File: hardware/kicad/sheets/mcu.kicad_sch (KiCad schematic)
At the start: 44 parts, among them J1 USB-C, J14 QWIIC, J5 DISPLAY, J6 NAV_SW, J7 AUX, SW1 RESET, SW2 BOOT, U1 ESP32-S3-WROOM-1U-N16R2, U4 SRV05-4

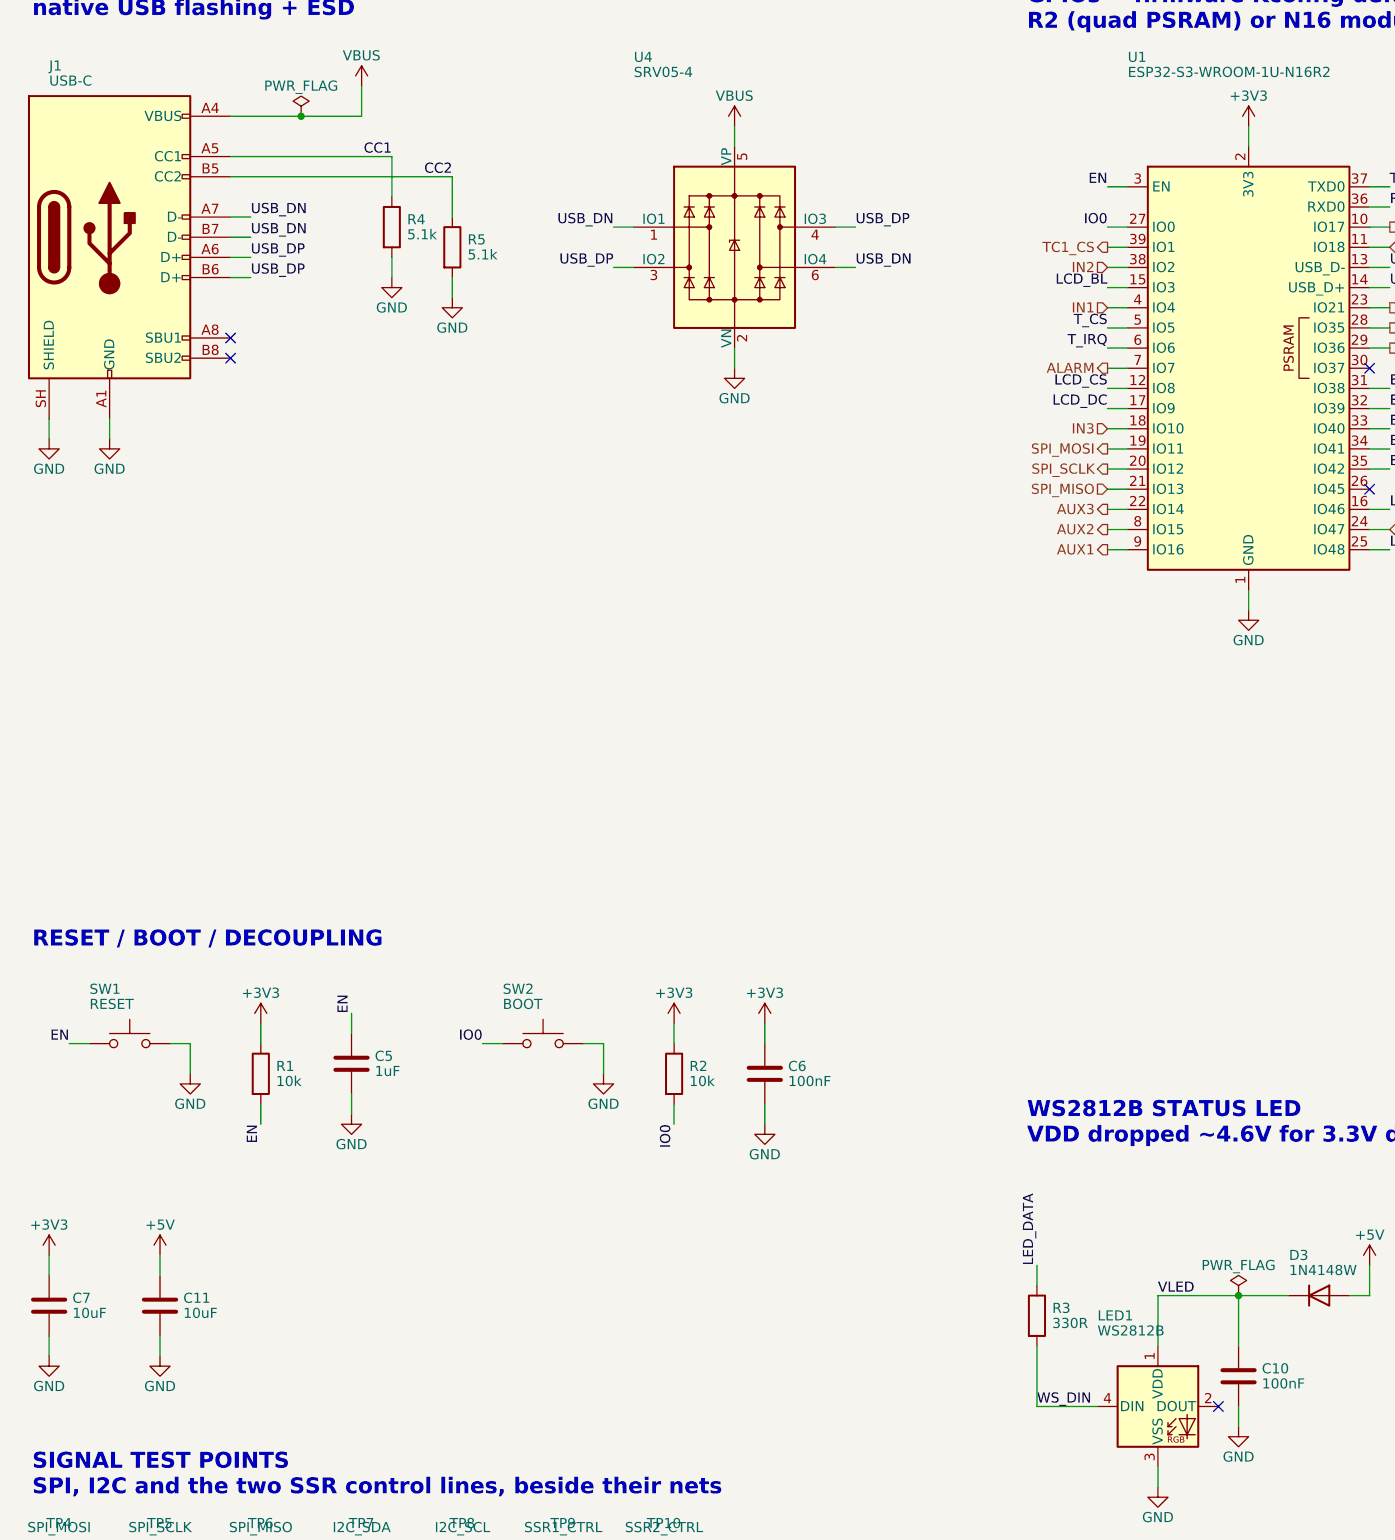
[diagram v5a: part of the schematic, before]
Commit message: hardware: inline front-ends and decoupling at the pins (review 12, 13)
Fourth batch from SCHEMATIC-REVIEW-2026-10-22.md.

Thermocouples: each MAX31856 front-end is an inline chain - the terminal
mirrored so its pins face the IC, K+ and K- on two lines through their
100R, the 100 nF differential cap bridging the lines, the 10 nF caps to
GND off each line, BIAS returned to the raw K- node along the bottom -
and AVDD/DVDD rise to a short +3V3 rail with both 100 nF hanging from
it. The ICs slid 7.62 mm right to make room; nothing else moved.

CT: J12 feeds four lines at 17.78 mm pitch with the 5R1 burden between
each pair, the 1k series parts in the path, the 33 nF to GND off each
filtered node and the 1k references off the N lines; the filtered nodes
end in the CTA_F / CTA_FN / CTB_F labels the ADE7953 pins already
carried. D6 keeps a label-fed clamp block beside the chain. VDD, VINTD
and VINTA each get a rail at the IC's top pin with their two caps on it;
R37/R38 moved 7.62 mm right to clear them.

io: IN1-IN3 are three identical rows - J11 mirrored, 1k in the path, the
10k pull-up above and 100 nF below the node, the hierarchical label at
the end - with D5's clamp block below them.

mcu: C6/C7 hang from U1's 3V3 pin. power: U2 is drawn as an inline
5 V -> 3.3 V chain with C1/C2 on its input and C3/C4 on its output in
the row the caps already occupied; LED2/R9 slid right.

Every pin landed on wiring by construction (the geometry helper checks
each symbol's pins against the wires), ERC is clean, the layout checker
reports no overlaps, the netlist still has 108 nets and the board sync
re-netted nothing. Fab outputs regenerated (schematic PDF, timestamps).

Co-Authored-By: Claude Fable 5.1 <noreply@anthropic.com>
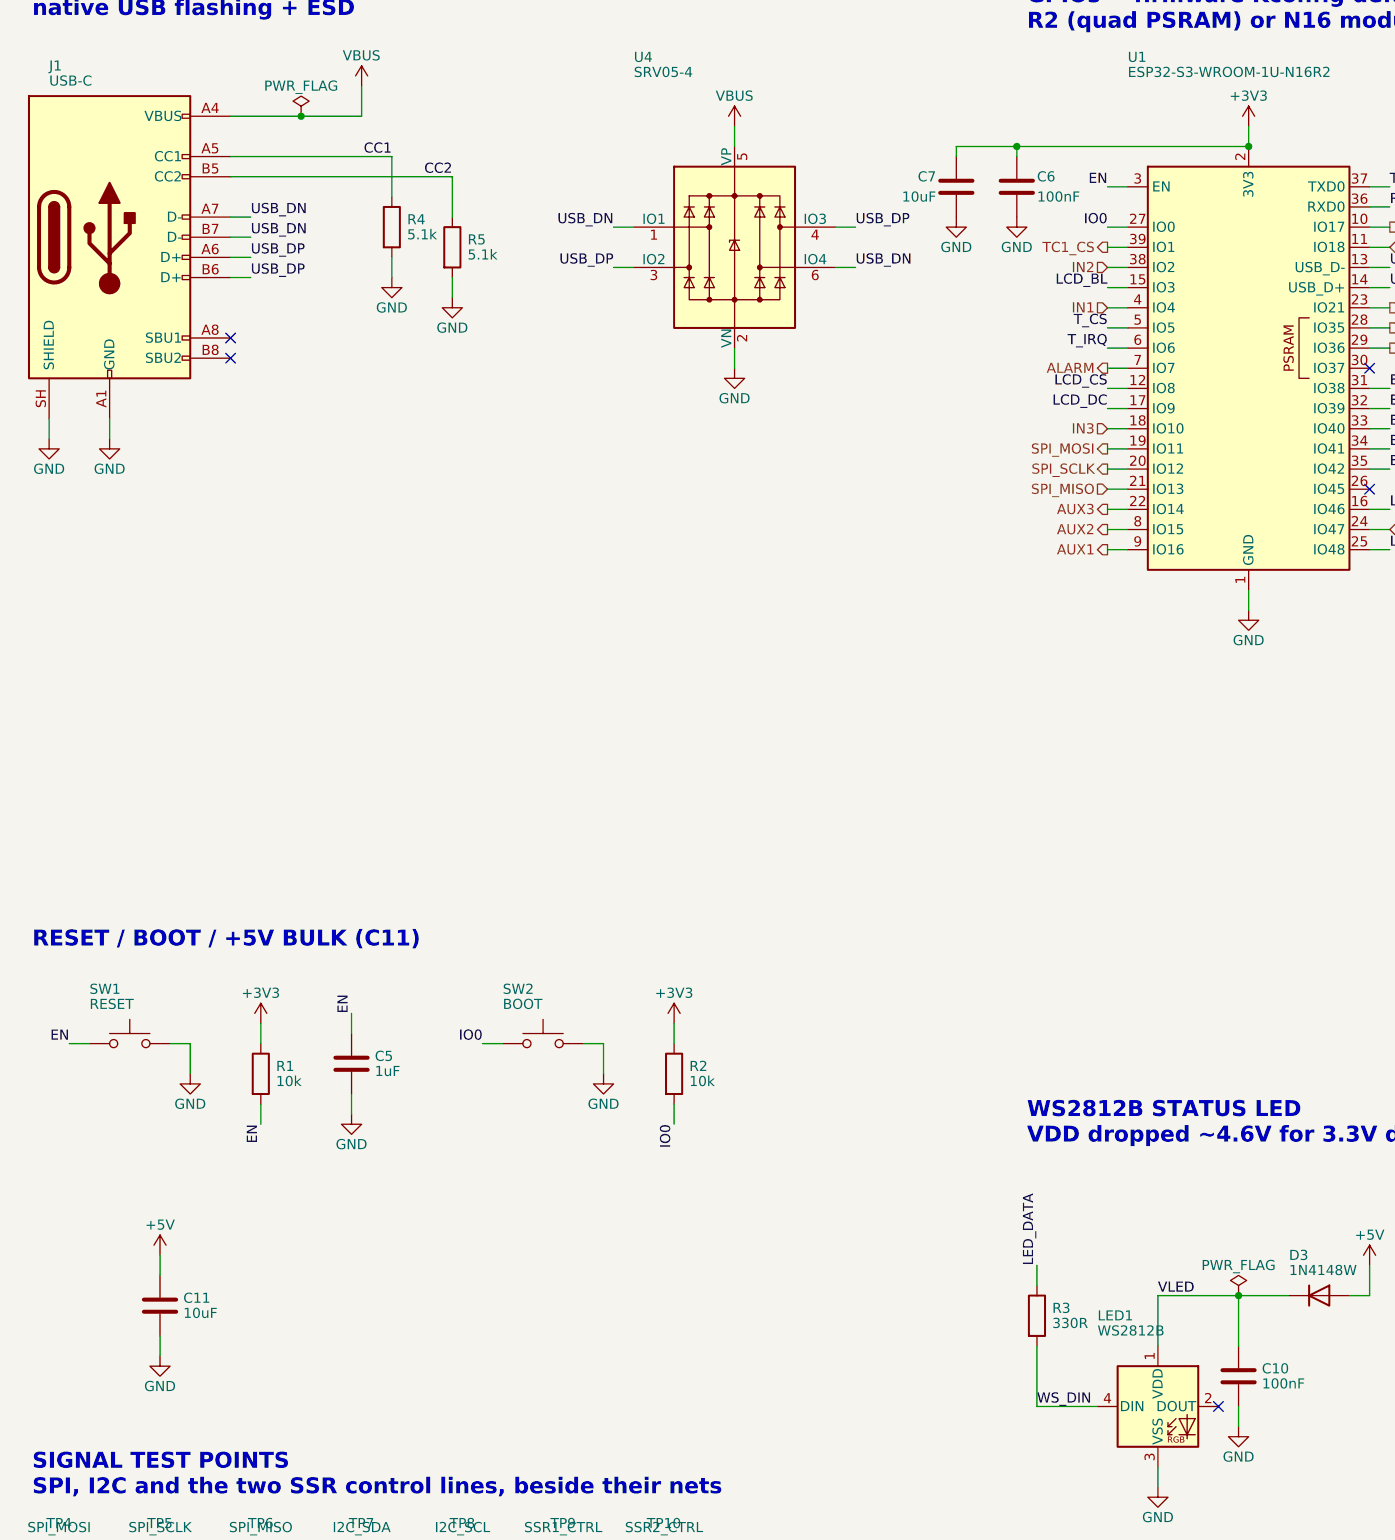
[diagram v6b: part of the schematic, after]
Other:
- note added: "RESET / BOOT / +5V BULK (C11)"
- note removed: "RESET / BOOT / DECOUPLING"
- moved on the sheet: C6, C7

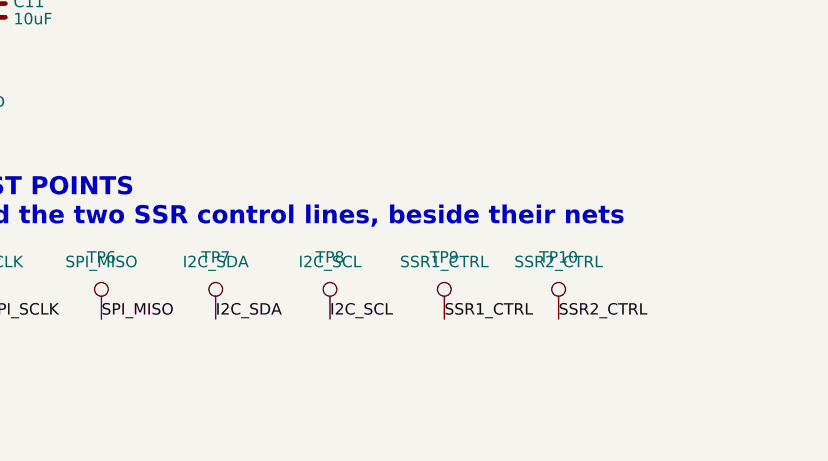
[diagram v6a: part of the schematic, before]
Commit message: hardware: drop the five test points a connector already exposes
TP1 (+3V3), TP2 (+5V), TP7/TP8 (I2C) and TP11 (CTA_P) each sat on a net
that a connector pin already reaches: +3V3 and I2C on the J7 AUX header
and J14 QWIIC, +5V on J5 pin 1, CTA_P on J12 pin 1. They are gone from
the test, mcu and ct sheets (TP3 and TP9/TP10 slide left into the gaps),
the board is synced, and the copper that only existed to reach them is
removed: eight segments and one via, 15.5 mm in all, most of it +5V's
spur from U2.3 up to the old TP2. DRC is 0 violations / 0 unconnected
with every severity on.

The seven that remain (TP3-TP6, TP9, TP10, TP12) probe nets nothing else
reaches, and none moved: on the board each already sits inline on its
net's route with at most a 0.4 mm jog. TP12 is the one with a real stub
(3.3 mm from R46.2), and SJ2's courtyard is what keeps it there.

TP_LEGEND_OK is empty again - dropping TP11 was the way out review A2
named. README, the bench smoke test (rails now probed at C2 / J7 pin 1),
gen_jlc's not-assembled set and the datasheet manifest follow. ERC 0,
make pcb-check ALL CHECKS PASS, SYNC IDEMPOTENT: PASS; fab outputs and
3D renders regenerated.

Co-Authored-By: Claude Fable 5.1 <noreply@anthropic.com>
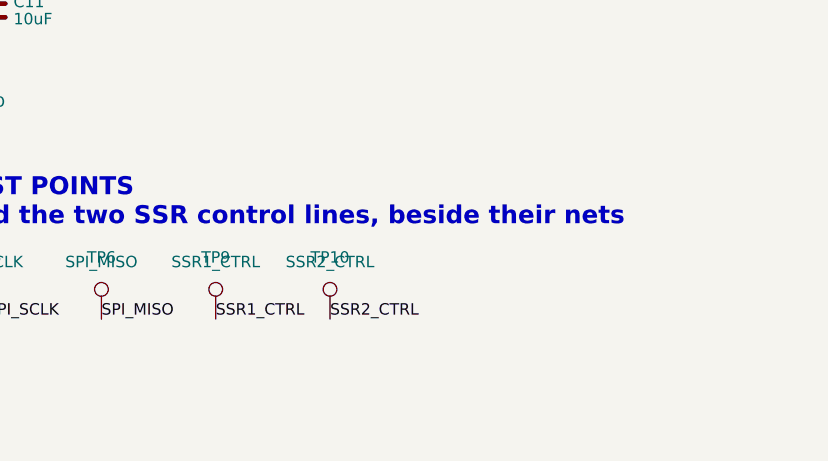
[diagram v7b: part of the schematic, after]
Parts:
- removed TP7: I2C_SDA, TestPoint:TestPoint_Pad_D1.0mm, symbol Connector:TestPoint
- removed TP8: I2C_SCL, TestPoint:TestPoint_Pad_D1.0mm, symbol Connector:TestPoint
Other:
- moved on the sheet: TP10, TP9
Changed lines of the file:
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@@
 		)
 	)
-	(label "I2C_SDA"
-		(at 63.5 228.6 0)
-		(effects
-			(font
-				(size 1.27 1.27)
-			)
-			(justify left bottom)
-		)
-	)
 	(label "LED_DATA"
 		(at 193.04 99.06 0)
@@
 	)
 	(label "SSR1_CTRL"
-		(at 88.9 228.6 0)
+		(at 63.5 228.6 0)
 		(effects
 			(font
@@
 		)
 	)
-	(label "I2C_SCL"
-		(at 76.2 228.6 0)
-		(effects
-			(font
-				(size 1.27 1.27)
-			)
-			(justify left bottom)
-		)
-	)
 	(label "T_CLK_R"
 		(at 335.28 189.23 270)
@@
 	)
 	(label "SSR2_CTRL"
-		(at 101.6 228.6 0)
+		(at 76.2 228.6 0)
 		(effects
 			(font
@@
 	)
 	(symbol
-		(lib_id "Connector:TestPoint")
-		(at 76.2 228.6 0)
-		(unit 1)
-		(body_style 1)
-		(exclude_from_sim no)
-		(in_bom yes)
-		(on_board yes)
-		(in_pos_files yes)
-		(dnp no)
-		(property "Reference" "TP8"
-			(at 76.2 221.742 0)
-			(show_name no)
-			(do_not_autoplace no)
-			(effects
-				(font
-					(size 1.27 1.27)
-				)
-			)
-		)
-		(property "Value" "I2C_SCL"
-			(at 76.2 222.25 0)
-			(show_name no)
-			(do_not_autoplace no)
-			(effects
-				(font
-					(size 1.27 1.27)
-				)
-			)
-		)
-		(property "Footprint" "TestPoint:TestPoint_Pad_D1.0mm"
-			(at 76.2 228.6 0)
-			(hide yes)
-			(show_name no)
-			(do_not_autoplace no)
-			(effects
-				(font
-					(size 1.27 1.27)
-				)
-			)
-		)
-		(property "Datasheet" ""
-			(at 76.2 228.6 0)
-			(hide yes)
-			(show_name no)
-			(do_not_autoplace no)
-			(effects
-				(font
-					(size 1.27 1.27)
-				)
-			)
-		)
-		(property "Description" "test point"
-			(at 76.2 228.6 0)
-			(hide yes)
-			(show_name no)
-			(do_not_autoplace no)
-			(effects
-				(font
-					(size 1.27 1.27)
-				)
-			)
-		)
-		(pin "1"
-		)
-		(instances
-			(project ""
-				(path "/1a47868a-bd78-50f4-b188-eb0464f4a928"
-					(reference "TP8")
-					(unit 1)
-				)
-			)
-		)
-	)
-	(symbol
 		(lib_id "Connector_Generic:Conn_01x08")
 		(at 378.46 52.07 0)
@@
 	(symbol
 		(lib_id "Connector:TestPoint")
-		(at 88.9 228.6 0)
-		(unit 1)
-		(body_style 1)
-		(exclude_from_sim no)
-		(in_bom yes)
-		(on_board yes)
-		(in_pos_files yes)
-		(dnp no)
-		(property "Reference" "TP9"
-			(at 88.9 221.742 0)
-			(show_name no)
-			(do_not_autoplace no)
-			(effects
-				(font
-					(size 1.27 1.27)
-				)
-			)
-		)
-		(property "Value" "SSR1_CTRL"
-			(at 88.9 222.25 0)
-			(show_name no)
-			(do_not_autoplace no)
-			(effects
-				(font
-					(size 1.27 1.27)
-				)
-			)
-		)
-		(property "Footprint" "TestPoint:TestPoint_Pad_D1.0mm"
-			(at 88.9 228.6 0)
-			(hide yes)
-			(show_name no)
-			(do_not_autoplace no)
-			(effects
-				(font
-					(size 1.27 1.27)
-				)
-			)
-		)
-		(property "Datasheet" ""
-			(at 88.9 228.6 0)
-			(hide yes)
-			(show_name no)
-			(do_not_autoplace no)
-			(effects
-				(font
-					(size 1.27 1.27)
-				)
-			)
-		)
-		(property "Description" "test point"
-			(at 88.9 228.6 0)
-			(hide yes)
-			(show_name no)
-			(do_not_autoplace no)
-			(effects
-				(font
-					(size 1.27 1.27)
-				)
-			)
-		)
-		(pin "1"
-		)
-		(instances
-			(project ""
-				(path "/1a47868a-bd78-50f4-b188-eb0464f4a928"
-					(reference "TP9")
-					(unit 1)
-				)
-			)
-		)
-	)
-	(symbol
-		(lib_id "Connector:TestPoint")
 		(at 63.5 228.6 0)
 		(unit 1)
@@
 		(in_pos_files yes)
 		(dnp no)
-		(property "Reference" "TP7"
+		(property "Reference" "TP9"
 			(at 63.5 221.742 0)
 			(show_name no)
@@
 			)
 		)
-		(property "Value" "I2C_SDA"
+		(property "Value" "SSR1_CTRL"
 			(at 63.5 222.25 0)
 			(show_name no)
@@
 			(project ""
 				(path "/1a47868a-bd78-50f4-b188-eb0464f4a928"
-					(reference "TP7")
+					(reference "TP9")
 					(unit 1)
 				)
@@
 	(symbol
 		(lib_id "Connector:TestPoint")
-		(at 101.6 228.6 0)
+		(at 76.2 228.6 0)
 		(unit 1)
 		(body_style 1)
@@
 		(dnp no)
 		(property "Reference" "TP10"
-			(at 101.6 221.742 0)
+			(at 76.2 221.742 0)
 			(show_name no)
 			(do_not_autoplace no)
@@
 		)
 		(property "Value" "SSR2_CTRL"
-			(at 101.6 222.25 0)
+			(at 76.2 222.25 0)
 			(show_name no)
 			(do_not_autoplace no)
@@
 		)
 		(property "Footprint" "TestPoint:TestPoint_Pad_D1.0mm"
-			(at 101.6 228.6 0)
+			(at 76.2 228.6 0)
 			(hide yes)
 			(show_name no)
@@
 		)
 		(property "Datasheet" ""
-			(at 101.6 228.6 0)
+			(at 76.2 228.6 0)
 			(hide yes)
 			(show_name no)
@@
 		)
 		(property "Description" "test point"
-			(at 101.6 228.6 0)
+			(at 76.2 228.6 0)
 			(hide yes)
 			(show_name no)

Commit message: hardware: the five quick fixes from the 2026-10-05/10-22 reviews
Schematic (rev B.3, sheets ct/power/mcu/ssr + root):
- R65, 1k from CTA_P to GND, mirrors R33 so the floating CT secondary
  sits at +-V/2 on IAP/IAN and channel A's pin limit is 139 A nominal,
  the same as channel B (schematic review 10-05 item 2).
- D9/D10 freewheel diodes are B5819W (JSCJ C8598, Basic, 1 A / 40 V,
  9 A surge) in the same SOD-123 land, replacing the 1N4148W whose
  150 mA rating never covered a 200 mA contactor coil (PCB review 10-05
  item 12). The SS34 was tried first and does not fit the SSR column.
- ADE_RESET is a hierarchical net to U1 IO37, the spare GPIO; the R30/C37
  RC stays for the power-on stretch (10-22 review E3).
- PWR_STATUS: BUCK_5V through R66 (100k) over R67+R68 (130k) to U1 IO45,
  2.8 V when the 24 V buck runs and 0 V on USB only (10-22 review E4).
  The TPS2116 ST pin would have said the same thing but its pad is boxed
  in by the USB pair on this layout, so it stays unconnected (C3, rev C).

Board:
- Every +5V layer transition (7) now has a second 0.6/0.3 via 0.85 mm
  away with a stub on each layer; the two in the USB corner use 0.3 mm
  stubs (fab-readiness C, "attempted, not landed" -> fixed).
- R65 placed below the CT filters; the divider in the two free columns
  south of U1, lifted 0.75 mm so the nameplate pocket keeps its 16.2 mm
  (it prints at 62% now). BUCK_5V tap hand-routed, the rest by the
  in-house router. DRC 0, make pcb-check ALL CHECKS PASS, 3D re-rendered.

Firmware/docs: KILN_PIN_ADE_RESET (37) and KILN_PIN_PWR_STATUS (45) in
Kconfig with the GPIO45 strapping caveat, check_pinmap NET_KCONFIG,
docs/pin-assignments.md (all 30 GPIOs assigned), DESIGN-NOTES sections
for each change, status notes in the four review documents, gen_jlc
sourcing + JLC_PLACEMENT rows, lcsc_pads cache and datasheet manifest.

Co-Authored-By: Claude Fable 5.1 <noreply@anthropic.com>
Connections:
- net PWR_STATUS: now reaches U1.26 (IO45)
- net ADE_RESET: now reaches U1.30 (IO37)
- no-connect marks 5 -> 3
